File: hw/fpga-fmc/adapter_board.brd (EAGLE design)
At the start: 69 x 84 mm, 115 parts, among them IC1 M24C02, J1 5569262-1, J2 ASP-134488-01, U1 ADM3066E, U10 ADM3066E, U11 ADM3066E, U12 ADM3066E, U13 ADM3066E, U14 ADM3066E, U15 ADM3066E, U16 ADM3066E, U17 TCA9548A, U2 ADM3066E, U3 ADM3066E, U4 ADM3066E, U5 ADM3066E, U6 ADM3066E, U7 ADM3066E, U8 ADM3066E, U9 ADM3066E

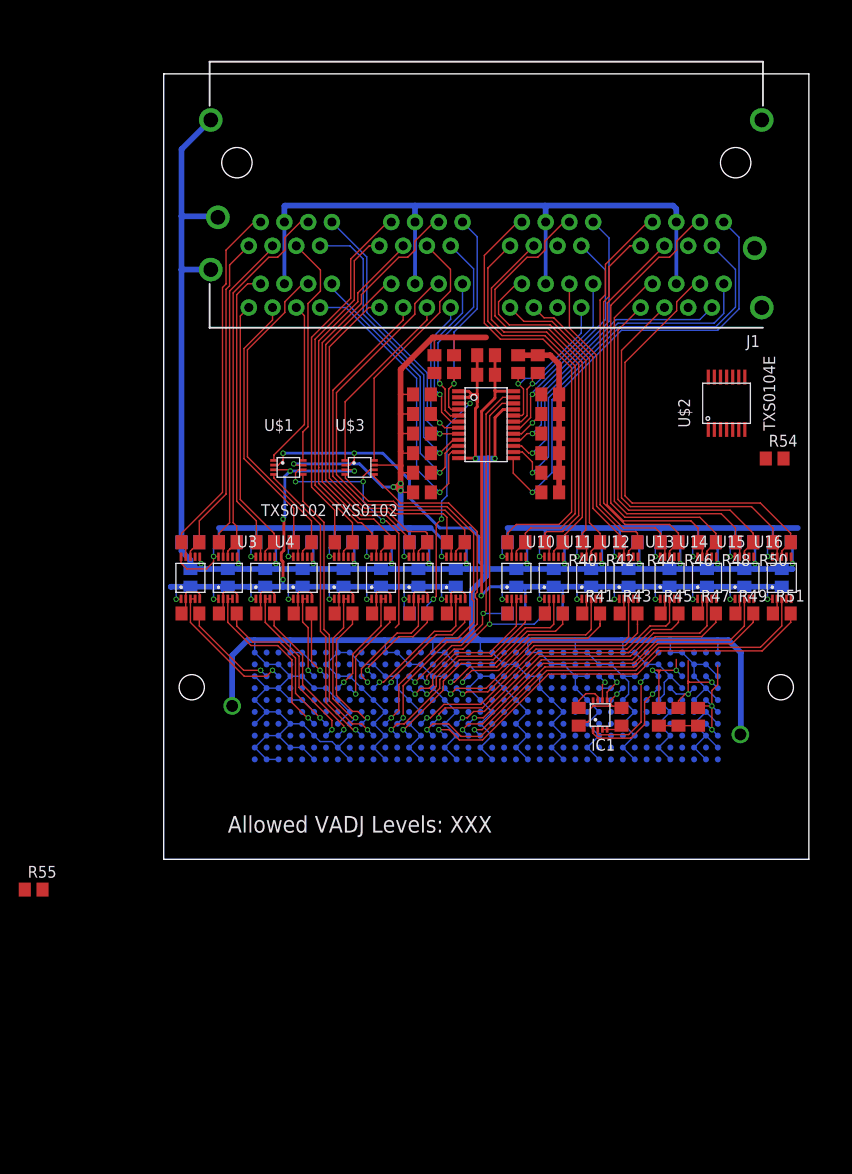
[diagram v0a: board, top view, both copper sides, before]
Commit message: fpga-fmc: route right side
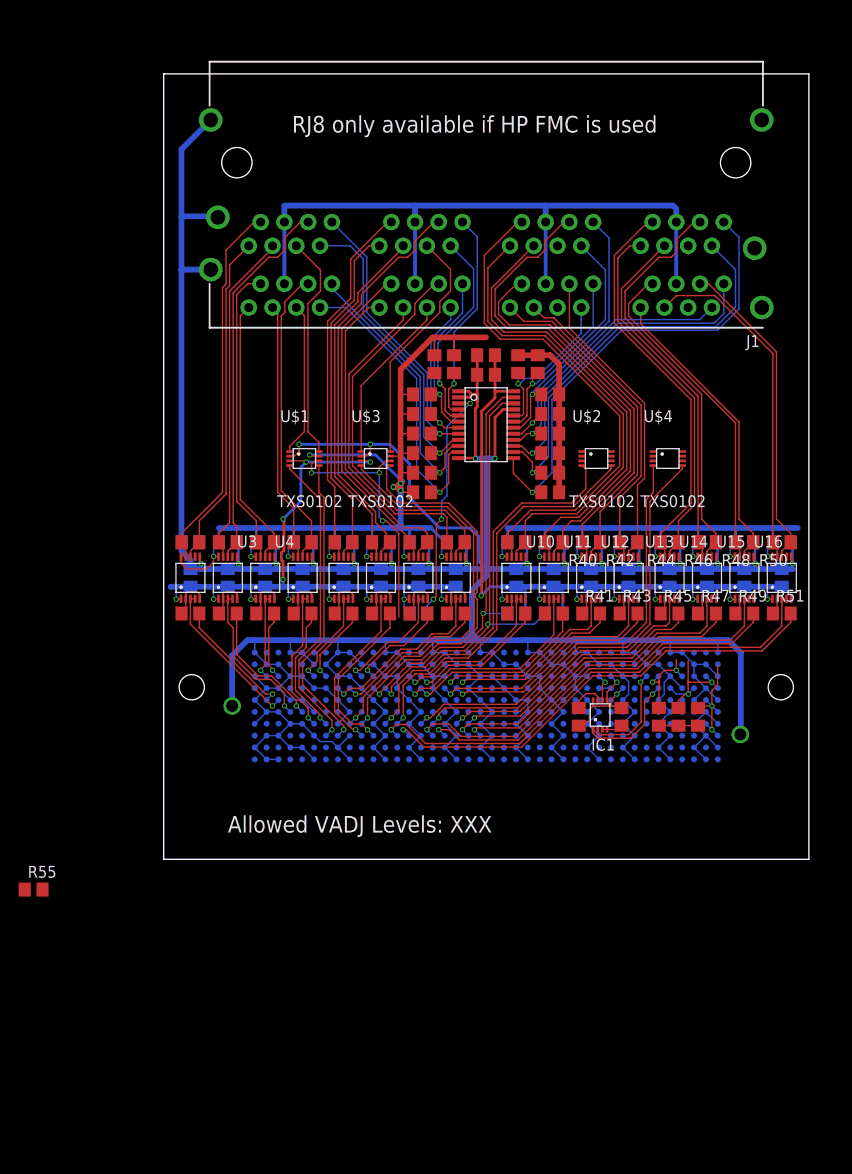
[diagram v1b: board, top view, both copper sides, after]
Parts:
- removed R54: (no value), rcl:R0805
- added U$4: TXS0102, parts:VSSOP-8
- U$2: value TXS0104E -> TXS0102; device parts:TSSOP-14 -> parts:VSSOP-8
- moved U$2 15.1 mm to (46.3, 42.9), turned to 0 degrees
- moved U$3 1.96 mm to (22.7, 42.9)
- moved U$1 1.96 mm to (15.0, 42.9)
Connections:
- removed net N$13: R54.2, U$2.8
- removed net N$2: U$2.5
- removed net N$3: U$2.4
- removed net N$4: U$2.3
- removed net N$5: U$2.2
- new net FMC_HA00_CC_N: J2.F5, R23.2
- new net FMC_HA00_CC_P: J2.F4, U2.P2, U2.P3
- new net FMC_HA01_CC_N: J2.E3, U1.P2, U1.P3
- new net FMC_HA01_CC_P: J2.E2, R2.2
- net 0V: now also U$2.2, U$4.2; no longer R54.1, U$2.7
- net 1V8: now also U$2.3, U$4.3; no longer U$2.1
- net 5V: now also U$2.7, U$4.7; no longer U$2.14
- net CONV_OE: now also U$2.6, U$4.6
- net FMC_DP0_C2M_N: now also R25.2; no longer U1.P2, U1.P3
- net FMC_DP0_C2M_P: now also U3.P2, U3.P3; no longer R2.2
- net FMC_DP0_M2C_N: now also R29.2; no longer R27.2
- net FMC_DP0_M2C_P: now also U5.P2, U5.P3; no longer U4.P2, U4.P3
- net FMC_LA00_CC_N: now also R27.2; no longer R23.2
- net FMC_LA00_CC_P: now also U4.P2, U4.P3; no longer U2.P2, U2.P3
- net FMC_LA01_CC_N: now also R35.2; no longer R31.2
- net FMC_LA01_CC_P: now also U8.P2, U8.P3; no longer U6.P2, U6.P3
- net FMC_LA02_N: now also U$1.5; no longer R25.2
- net FMC_LA02_P: now also U$1.4; no longer U3.P2, U3.P3
- net FMC_LA03_N: now also U$3.5; no longer R29.2
- net FMC_LA03_P: now also U$3.4; no longer U5.P2, U5.P3
- net FMC_LA04_N: now also R31.2; no longer U$1.5
- net FMC_LA04_P: now also U6.P2, U6.P3; no longer U$1.4
- net FMC_LA05_N: now also R6.1, U17.P21; no longer R35.2
- net FMC_LA05_P: now also R5.1, U17.P22; no longer U8.P2, U8.P3
- net FMC_LA07_N: now also R51.2; no longer R39.2
- net FMC_LA07_P: now also U16.P2, U16.P3; no longer U10.P2, U10.P3
- net FMC_LA08_N: now also U$2.5; no longer U$3.5
- net FMC_LA08_P: now also U$2.4; no longer U$3.4
- net FMC_LA09_N: now also R39.2; no longer R37.2
- net FMC_LA09_P: now also U10.P2, U10.P3; no longer U9.P2, U9.P3
- net FMC_LA10_N: now also R37.2; no longer R6.1, U17.P21
- net FMC_LA10_P: now also U9.P2, U9.P3; no longer R5.1, U17.P22
- net FMC_LA11_N: now also R49.2; no longer R51.2
- net FMC_LA11_P: now also U15.P2, U15.P3; no longer U16.P2, U16.P3
- net FMC_LA12_N: now also U$4.5; no longer R45.2
- net FMC_LA12_P: now also U$4.4; no longer U13.P2, U13.P3
- net FMC_LA15_N: now also R47.2; no longer R49.2
- net FMC_LA15_P: now also U14.P2, U14.P3; no longer U15.P2, U15.P3
- net FMC_LA16_N: now also R45.2; no longer R47.2
- net FMC_LA16_P: now also U13.P2, U13.P3; no longer U14.P2, U14.P3
- net RJ1_CONV: now also U$4.8; no longer U$2.10
- net RJ2_CONV: now also U$2.8; no longer U$2.13
- net RJ5_CONV: now also U$4.1; no longer U$2.11
- net RJ6_CONV: now also U$2.1; no longer U$2.12
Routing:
- net FMC_LA05_N: track 12.5 -> 47.0 mm, vias 1 -> 2
- net FMC_LA05_P: track 15.0 -> 44.2 mm, vias 1 -> 2
- net FMC_LA03_P: track 15.8 -> 43.7 mm
- net FMC_LA03_N: track 15.1 -> 42.5 mm
- net FMC_LA10_N: track 42.3 -> 15.0 mm, vias 2 -> 1
- net FMC_LA07_P: track 26.2 -> 52.3 mm
- net FMC_LA07_N: track 24.3 -> 49.6 mm
- net FMC_LA10_P: track 39.6 -> 17.6 mm, vias 2 -> 1
- net FMC_HA01_CC_N: track 0.00 -> 16.5 mm, vias 0 -> 1
- net FMC_HA00_CC_P: track 0.00 -> 16.2 mm, vias 0 -> 1
- net FMC_LA02_N: track 16.4 -> 32.1 mm
- net FMC_LA02_P: track 18.3 -> 32.9 mm
- net RJ1_DATA_P: track 48.6 -> 34.1 mm
- net FMC_LA12_N: track 31.9 -> 46.3 mm
- net FMC_HA00_CC_N: track 0.00 -> 14.3 mm, vias 0 -> 1
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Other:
- board text added: "RJ8 only available if HP FMC is used"

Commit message: hw/fpga-fmc: add 5V supply and route remaining CONV signals
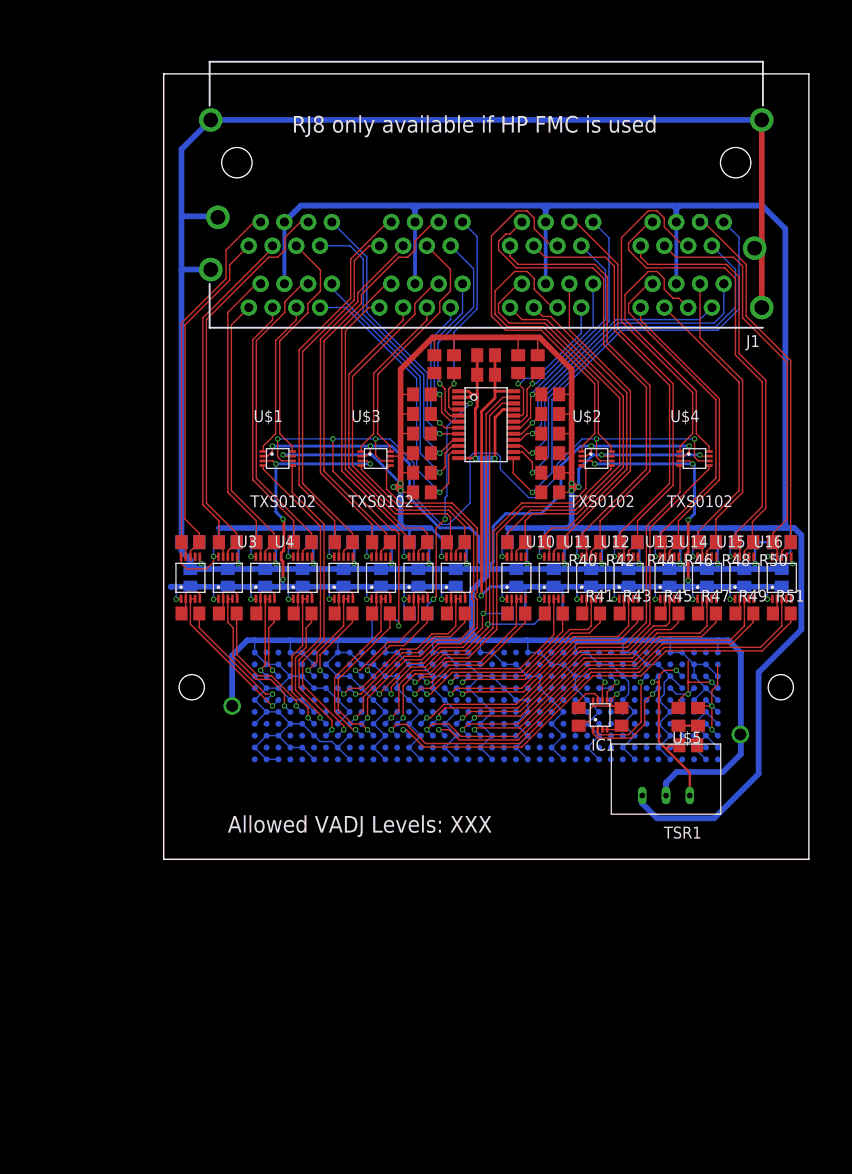
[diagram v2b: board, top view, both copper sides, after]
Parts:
- added U$5: TSR1, parts:TSR1
- moved R55 47.5 mm to (23.2, 26.3), flipped to the bottom, turned to 180 degrees
- moved C37 4.38 mm to (56.1, 12.2), turned to 180 degrees
- moved U$4 2.86 mm to (56.8, 42.9)
- moved U$1 2.86 mm to (12.2, 42.9)
- turned C34 to 0 degrees
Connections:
- net +12V: now also U$5.P1; no longer J1.1.4, J1.2.4, J1.3.4, J1.4.4, J1.5.4, J1.6.4, J1.7.4, J1.8.4
- net 0V: now also U$5.P2
- net 5V: now also J1.1.4, J1.2.4, J1.3.4, J1.4.4, J1.5.4, J1.6.4, J1.7.4, J1.8.4, U$5.P3
- net RJ1_CLK_N: now also R44.2, U13.P8; no longer R48.2, U15.P8
- net RJ1_CLK_P: now also R44.1, U13.P7; no longer R48.1, U15.P7
- net RJ1_DATA_N: now also R46.2, U14.P8; no longer R50.2, U16.P8
- net RJ1_DATA_P: now also R46.1, U14.P7; no longer R50.1, U16.P7
- net RJ2_CLK_N: now also R36.2, U9.P8; no longer R40.2, U11.P8
- net RJ2_CLK_P: now also R36.1, U9.P7; no longer R40.1, U11.P7
- net RJ2_DATA_N: now also R38.2, U10.P8; no longer R42.2, U12.P8
- net RJ2_DATA_P: now also R38.1, U10.P7; no longer R42.1, U12.P7
- net RJ5_CLK_N: now also R48.2, U15.P8; no longer R44.2, U13.P8
- net RJ5_CLK_P: now also R48.1, U15.P7; no longer R44.1, U13.P7
- net RJ5_DATA_N: now also R50.2, U16.P8; no longer R46.2, U14.P8
- net RJ5_DATA_P: now also R50.1, U16.P7; no longer R46.1, U14.P7
- net RJ6_CLK_N: now also R40.2, U11.P8; no longer R36.2, U9.P8
- net RJ6_CLK_P: now also R40.1, U11.P7; no longer R36.1, U9.P7
- net RJ6_DATA_N: now also R42.2, U12.P8; no longer R38.2, U10.P8
- net RJ6_DATA_P: now also R42.1, U12.P7; no longer R38.1, U10.P7
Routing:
- net 5V: track 193.3 -> 407.5 mm, vias 19 -> 24
- net 0V: track 602.4 -> 734.3 mm, vias 20 -> 22
- net CONV_OE: track 27.7 -> 102.1 mm, vias 3 -> 6
- net +12V: track 84.6 -> 20.5 mm
- net RJ6_CONV: track 0.00 -> 40.8 mm
- net RJ5_CONV: track 0.95 -> 37.0 mm
- net RJ2_CONV: track 0.00 -> 34.3 mm
- net RJ1_CONV: track 0.00 -> 30.5 mm
- net 1V8: track 153.3 -> 182.6 mm, vias 21 -> 25
- net RJ6_DATA_P: track 52.6 -> 42.8 mm
- net RJ5_CLK_N: track 42.7 -> 49.2 mm
- net RJ5_CLK_P: track 39.4 -> 44.8 mm
- net RJ1_DATA_N: track 36.6 -> 32.0 mm
- net RJ2_CLK_P: track 36.1 -> 40.7 mm
- net RJ5_DATA_N: track 38.7 -> 43.1 mm
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
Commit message: hw/fpga-fmc: finalize pcb design and prepare BOM
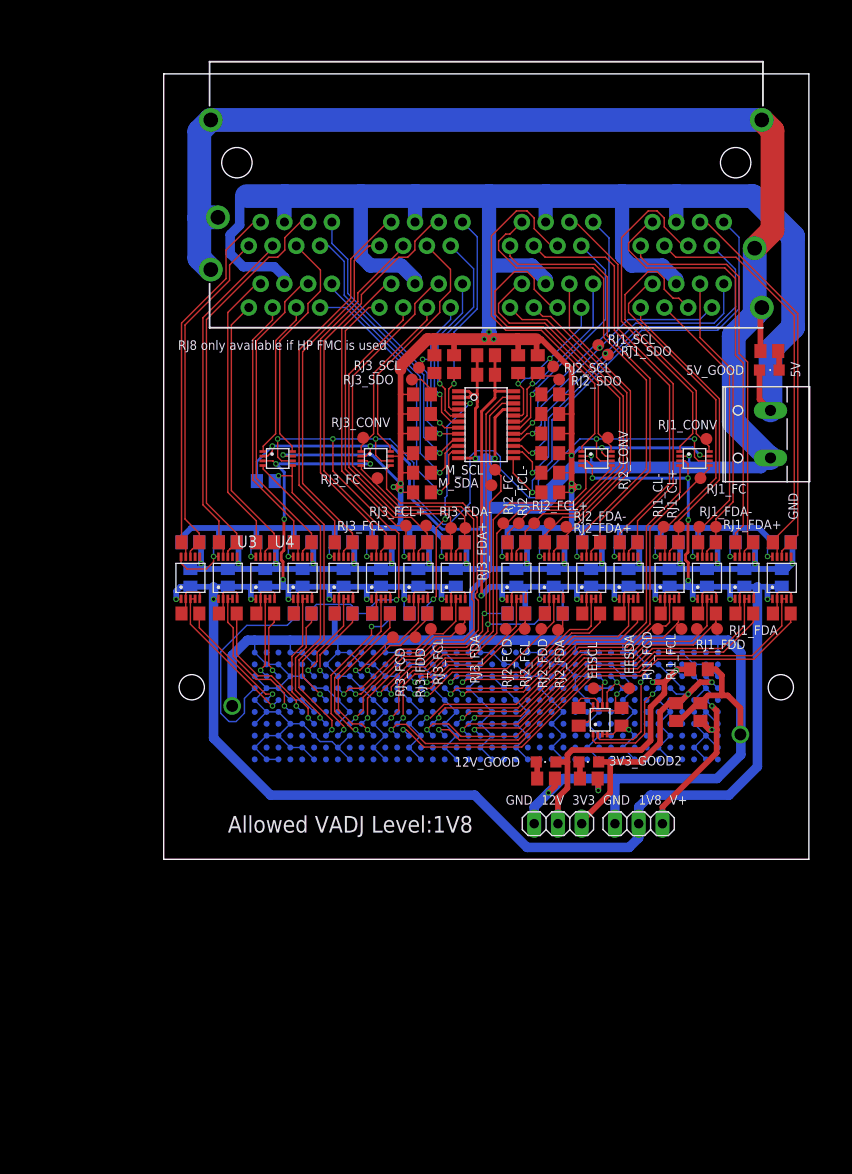
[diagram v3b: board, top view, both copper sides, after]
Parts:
- removed U$5: TSR1, parts:TSR1
- added 12V_GOOD, 3V3_GOOD2, 5V_GOOD: (no value), led:CHIPLED_0805
- added EESCL, EESDA, M_SCL, M_SDA, RJ1_CL+, RJ1_CL-, RJ1_CONV, RJ1_FC, RJ1_FCD, RJ1_FCL, RJ1_FDA, RJ1_FDA+, RJ1_FDA-, RJ1_FDD, RJ1_SCL, RJ1_SDO, RJ2_CONV, RJ2_FC, RJ2_FCD, RJ2_FCL, RJ2_FCL+, RJ2_FCL-, RJ2_FDA, RJ2_FDA+, RJ2_FDA-, RJ2_FDD, RJ2_SCL, RJ2_SDO, RJ3_CONV, RJ3_FC, RJ3_FCD, RJ3_FCL, RJ3_FCL+, RJ3_FCL-, RJ3_FDA, RJ3_FDA+, RJ3_FDA-, RJ3_FDD, RJ3_SCL, RJ3_SDO: TPB1,27, testpad:B1,27
- added J3, J4: (no value), pinhead:1X03
- added R53: 330R, resistor:R0805
- added R54: 1k, resistor:R0805
- added R56: 130R, resistor:R0805
- added R57, R58: 0R, rcl:R0805
- added R59: NB, rcl:R0805
- added X1: (no value), con-wago-508:W237-132
- R1, R22, R24, R26, R28, R30, R32, R34, R36, R38, R40, R42, R44, R46, R48, R50: value (none) -> 120R
- R10, R11, R12, R13, R14, R15, R16, R17, R18, R19, R20, R21, R3, R4, R5, R6, R8, R9: value 1k -> 4k
- R55: value (none) -> 10k
- moved C37 8.21 mm to (57.2, 20.3)
- moved R55 4.00 mm to (19.2, 26.3)
- moved C35 0.57 mm to (57.4, 15.7), turned to 270 degrees
- moved C36 0.57 mm to (54.8, 15.7)
- moved IC1 0.51 mm to (46.7, 14.9)
- turned C2 to 180 degrees
- turned C34 to 180 degrees
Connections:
- new net FMC_HA05_N: J2.E7, R59.1, U$1.5
- new net N$2: 12V_GOOD.C, R54.2
- new net N$3: 3V3_GOOD2.C, R56.2
- new net N$5: 5V_GOOD.C, R53.2
- net +12V: now also 12V_GOOD.A, J3.2; no longer U$5.P1
- net +3V3: now also 3V3_GOOD2.A, J3.1
- net 0V: now also J3.3, J4.3, R53.1, R54.1, R56.1, R59.2, X1.1; no longer U$5.P2
- net 1V8: now also J4.2
- net 1V8_POWER_GOOD: now also R58.1
- net 5V: now also 5V_GOOD.A, X1.2; no longer U$5.P3
- net CONV_OE: now also R57.1, R58.2
- net FMC_IIC_SCL: now also EESCL.TP
- net FMC_IIC_SDA: now also EESDA.TP
- net FMC_LA01_CC_N: now also RJ3_FDA.TP
- net FMC_LA01_CC_P: now also RJ3_FDD.TP
- net FMC_LA02_N: now also R57.2; no longer U$1.5
- net FMC_LA03_P: now also RJ3_FC.TP
- net FMC_LA05_N: now also M_SCL.TP
- net FMC_LA05_P: now also M_SDA.TP
- net FMC_LA06_N: now also RJ3_FCL.TP
- net FMC_LA06_P: now also RJ3_FCD.TP
- net FMC_LA08_N: now also RJ2_FC.TP
- net FMC_LA09_N: now also RJ2_FDA.TP
- net FMC_LA09_P: now also RJ2_FDD.TP
- net FMC_LA10_N: now also RJ2_FCL.TP
- net FMC_LA10_P: now also RJ2_FCD.TP
- net FMC_LA12_N: now also RJ1_FC.TP
- net FMC_LA15_N: now also RJ1_FDA.TP
- net FMC_LA15_P: now also RJ1_FDD.TP
- net FMC_LA16_N: now also RJ1_FCL.TP
- net FMC_LA16_P: now also RJ1_FCD.TP
- net RJ1_CLK_N: now also RJ1_CL-.TP
- net RJ1_CLK_P: now also RJ1_CL+.TP
- net RJ1_CONV: now also RJ1_CONV.TP
- net RJ1_DATA_N: now also RJ1_FDA-.TP
- net RJ1_DATA_P: now also RJ1_FDA+.TP
- net RJ1_SCL: now also RJ1_SCL.TP
- net RJ1_SDO: now also RJ1_SDO.TP
- net RJ2_CLK_N: now also RJ2_FCL-.TP
- net RJ2_CLK_P: now also RJ2_FCL+.TP
- net RJ2_CONV: now also RJ2_CONV.TP
- net RJ2_DATA_N: now also RJ2_FDA-.TP
- net RJ2_DATA_P: now also RJ2_FDA+.TP
- net RJ2_SCL: now also RJ2_SCL.TP
- net RJ2_SDO: now also RJ2_SDO.TP
- net RJ3_CLK_N: now also RJ3_FCL-.TP
- net RJ3_CLK_P: now also RJ3_FCL+.TP
- net RJ3_CONV: now also RJ3_CONV.TP
- net RJ3_DATA_N: now also RJ3_FDA-.TP
- net RJ3_DATA_P: now also RJ3_FDA+.TP
- net RJ3_SCL: now also RJ3_SCL.TP
- net RJ3_SDO: now also RJ3_SDO.TP
- net V+: now also J4.1
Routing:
- net 1V8: track 182.6 -> 285.8 mm
- net FMC_HA05_N: track 0.00 -> 30.7 mm, vias 0 -> 2
- net 0V: track 734.3 -> 764.1 mm, vias 22 -> 25
- net 1V8_POWER_GOOD: track 0.00 -> 22.8 mm
- net +3V3: track 13.3 -> 30.3 mm
- net FMC_LA02_N: track 33.3 -> 17.2 mm, vias 1 -> 2
- net +12V: track 20.5 -> 31.8 mm
- net V+: track 12.3 -> 20.9 mm
- net CONV_OE: track 102.1 -> 109.6 mm
- net 5V: track 407.5 -> 403.9 mm, vias 24 -> 28
- net RJ3_SDO: track 18.5 -> 21.6 mm
- net LSIO13: track 1.75 -> 4.58 mm
- net LSIO11: track 1.75 -> 4.58 mm
- net LSIO9: track 1.75 -> 4.58 mm
- net LSIO15: track 1.75 -> 4.58 mm
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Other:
- board text added: "12V"
- board text added: "1V8"
- board text added: "3V3"
- board text added: "5V"
- board text added: "Allowed VADJ Level:1V8"
- board text added: "GND"
- board text added: "V+"
- board text removed: "Allowed VADJ Levels: XXX"

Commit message: hw/fpga-fmc: fix clearance issues
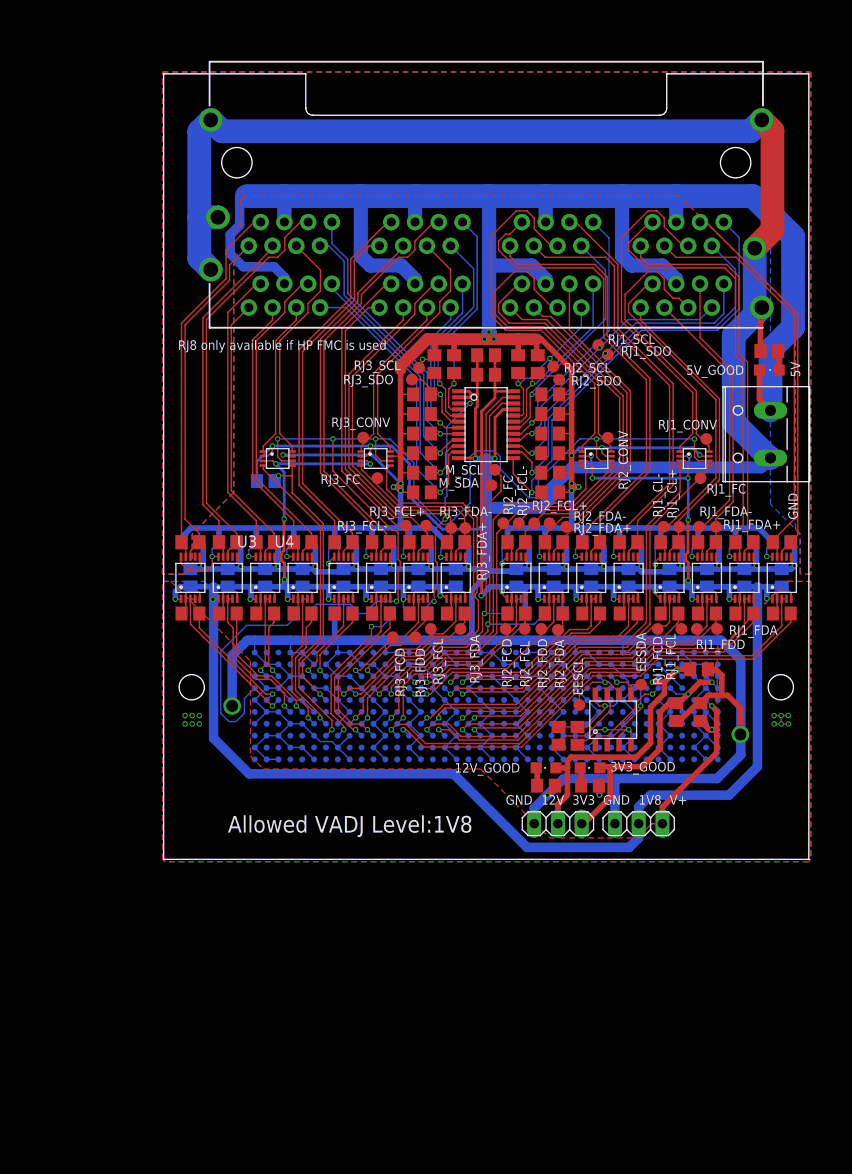
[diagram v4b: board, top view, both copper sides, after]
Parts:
- removed 3V3_GOOD2: (no value), led:CHIPLED_0805
- added 3V3_GOOD: (no value), led:CHIPLED_0805
- IC1: device parts:8-VFSOP -> parts:SO8N
- R10, R11, R12, R13, R14, R15, R16, R17, R18, R19, R20, R21, R3, R4, R5, R6, R8, R9: value 4k -> 4.7k
- R52: value 0R -> NB
- moved C39 5.12 mm to (44.3, 13.2)
- moved R52 2.96 mm to (42.2, 13.2), turned to 90 degrees
- moved EESCL 2.34 mm to (44.5, 16.5)
- moved IC1 1.40 mm to (48.1, 14.9)
- moved EESDA 1.33 mm to (51.1, 18.7)
- moved R56 0.77 mm to (45.6, 7.87)
- moved R54 0.76 mm to (40.9, 7.87)
- moved 12V_GOOD 0.63 mm to (40.9, 9.78)
- renumbered U$1 to U18, U$2 to U20, U$3 to U19, U$4 to U21
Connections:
- net +3V3: now also 3V3_GOOD.A; no longer 3V3_GOOD2.A
- net N$3: now also 3V3_GOOD.C; no longer 3V3_GOOD2.C
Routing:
- net 0V: track 764.1 -> 783.7 mm, vias 25 -> 38
- net 5V: track 403.9 -> 409.7 mm
- net N$1: track 3.45 -> 9.14 mm
- net FMC_IIC_SCL: track 4.43 -> 7.74 mm
- net GA0: track 11.6 -> 9.10 mm
- net 3P3VAUX: track 9.10 -> 11.4 mm
- net GA1: track 12.2 -> 10.0 mm
- net FMC_IIC_SDA: track 5.38 -> 4.60 mm
- added copper zone on layer 1, net 0V
- added copper zone on layer 16, net 0V
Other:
- outline, holes or cut-outs redrawn
